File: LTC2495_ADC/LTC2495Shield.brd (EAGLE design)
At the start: 39.7 x 26.7 mm, 5 parts

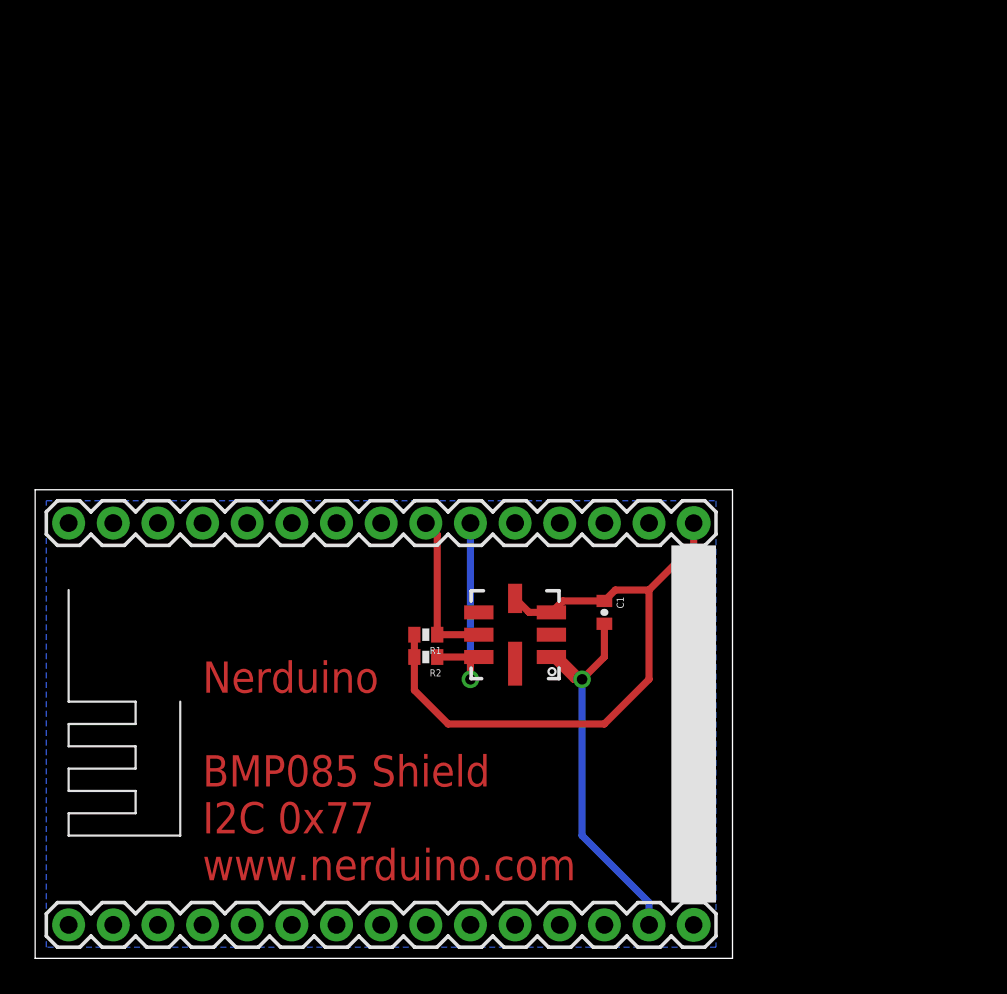
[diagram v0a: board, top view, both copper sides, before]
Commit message: Updated BMP180 symbol Removed BMP085 shield (redundant) Added DS3231 RTC Shield Added LTC2495 ADC Shield Added chip data sheets for each shield
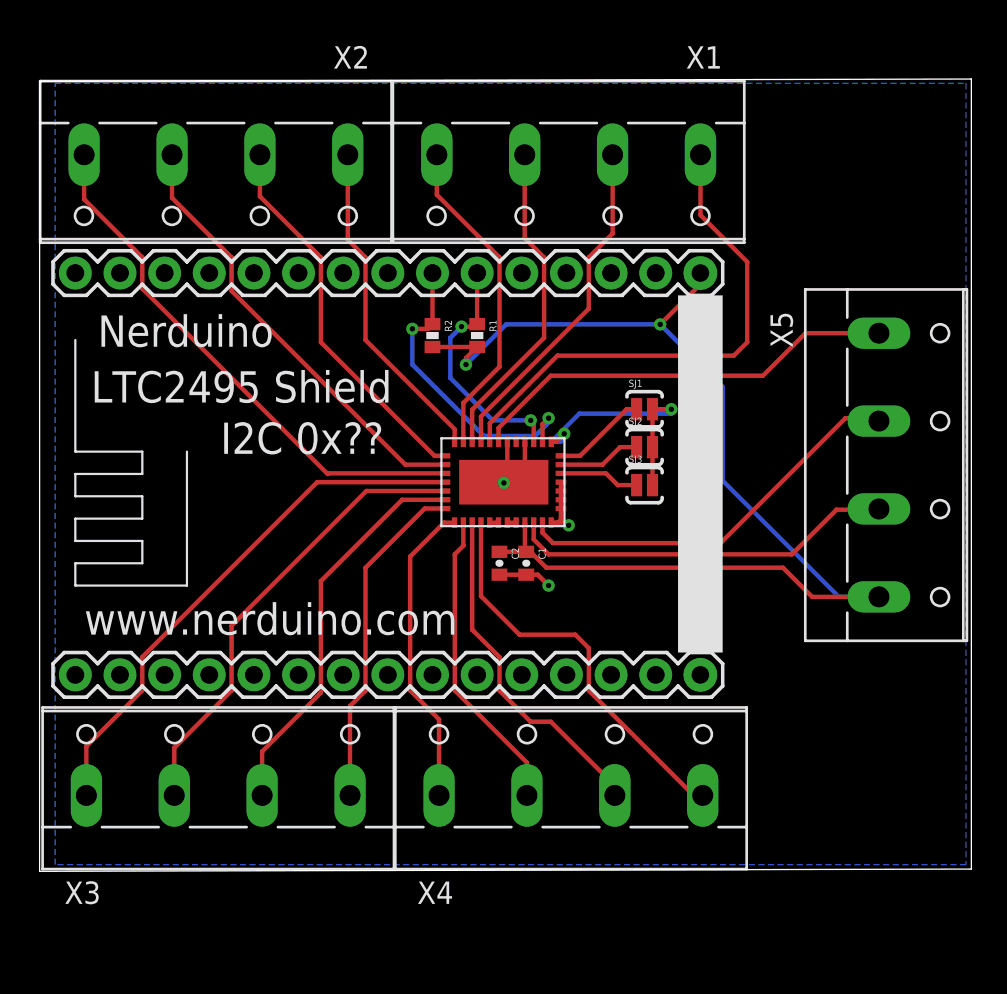
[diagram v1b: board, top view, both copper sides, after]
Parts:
- removed U$2: BMP085, SparkFun:BMP085
- added C2: 1uF, SparkFun:0402-CAP
- added SJ1, SJ2, SJ3: SOLDERJUMPERNO, SparkFun:SJ_2S-NO
- added U$3: LTC2495, SparkFun-AnalogIC:UHF38
- added X1, X2, X3, X4, X5: (no value), con-wago-500:W237-4
- moved R2 18.3 mm to (22.0, 34.8), turned to 270 degrees
- moved R1 17.3 mm to (24.5, 34.8), turned to 270 degrees
- moved U$1 14.2 mm to (19.4, 20.6)
- moved C1 5.25 mm to (27.3, 21.8)
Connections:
- new net N$10: U$3.P$14, X2.3
- new net N$11: U$3.P$15, X2.4
- new net N$12: U$3.P$16, X3.1
- new net N$13: U$3.P$17, X3.2
- new net N$14: U$3.P$18, X3.3
- new net N$15: U$3.P$19, X3.4
- new net N$16: U$3.P$20, X4.1
- new net N$17: U$3.P$21, X4.2
- new net N$18: U$3.P$22, X4.3
- new net N$19: U$3.P$23, X4.4
- new net N$20: SJ1.1, U$3.P$38
- new net N$21: SJ2.1, U$3.P$37
- new net N$22: SJ3.1, U$3.P$36
- new net N$25: U$3.P$7, X5.1
- new net N$26: U$3.P$29, X5.3
- new net N$27: U$3.P$30, X5.2
- new net N$28: U$3.P$26, U$3.P$27
- new net N$29: U$3.P$24, U$3.P$25
- new net N$4: U$3.P$9, X1.2
- new net N$5: U$3.P$10, X1.3
- new net N$6: U$3.P$11, X1.4
- new net N$7: U$3.P$12, X2.1
- new net N$8: R2.1, U$1.22, U$3.P$2
- new net N$9: U$3.P$13, X2.2
- net 3.3V: now also C2.1, U$3.P$28, X5.4; no longer U$2.3, U$2.4
- net GND: now also C2.2, SJ1.2, SJ2.2, SJ3.2, U$3.P$1, U$3.P$31, U$3.P$32, U$3.P$33, U$3.P$34, U$3.P$35, U$3.P$39, U$3.P$4, U$3.P$6; no longer U$2.1
- net N$2: now also R1.1, U$3.P$3; no longer R2.1, U$2.7
- net N$3: now also U$3.P$8, X1.1; no longer R1.1, U$1.22, U$2.6
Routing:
- net N$11: track 0.00 -> 30.6 mm
- net N$12: track 0.00 -> 30.5 mm
- net 3.3V: track 36.8 -> 66.0 mm, vias 0 -> 2
- net N$13: track 0.00 -> 26.3 mm
- net N$10: track 0.00 -> 25.4 mm
- net N$25: track 0.00 -> 24.7 mm
- net N$27: track 0.00 -> 23.0 mm
- net N$19: track 0.00 -> 22.9 mm
- net N$14: track 0.00 -> 22.6 mm
- net N$26: track 0.00 -> 22.0 mm
- net N$9: track 0.00 -> 21.8 mm
- net N$3: track 8.98 -> 29.4 mm
- net N$18: track 0.00 -> 19.6 mm
- net N$4: track 0.00 -> 19.4 mm
- net N$15: track 0.00 -> 19.2 mm
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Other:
- board size 39.7 x 26.7 mm -> 53 x 45.1 mm
- board text added: "I2C 0x??"
- board text added: "LTC2495 Shield"
- board text added: "Nerduino"
- board text added: "www.nerduino.com"
- board text removed: "Nerduino BMP085 Shield I2C 0x77 www.nerduino.com"
